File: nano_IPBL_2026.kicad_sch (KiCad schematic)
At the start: 21 parts, among them J1 DB301V-5.0-2P, M1 Motor_Servo, M10 Motor_Servo, M11 Motor_Servo, M12 Motor_Servo, M2 Motor_Servo, M3 Motor_Servo, M4 Motor_Servo, M5 Motor_Servo, M6 Motor_Servo, M7 Motor_Servo, M8 Motor_Servo, M9 Motor_Servo

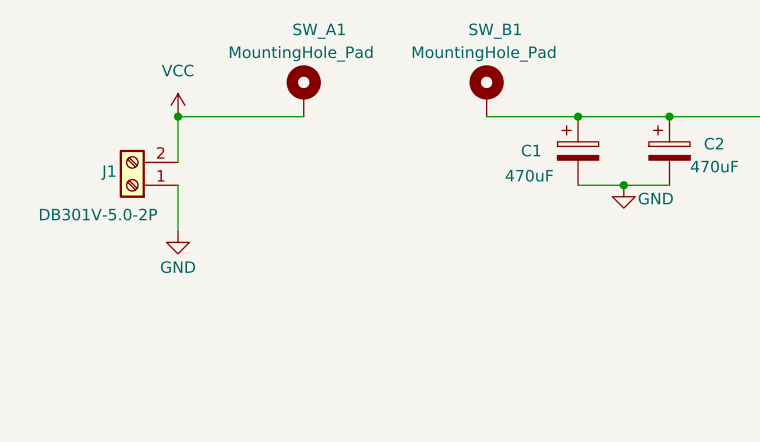
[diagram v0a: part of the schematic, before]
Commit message: Update screw terminal footprint and replace SW_A1/SW_B1 mounting holes with header
Screw terminal footprint now includes its 3D model counterpart. SW_A1
and SW_B1 mounting holes replaced with a 1-pin connected header.
Copper/silkscreen layer view colors changed from inverted to colored.
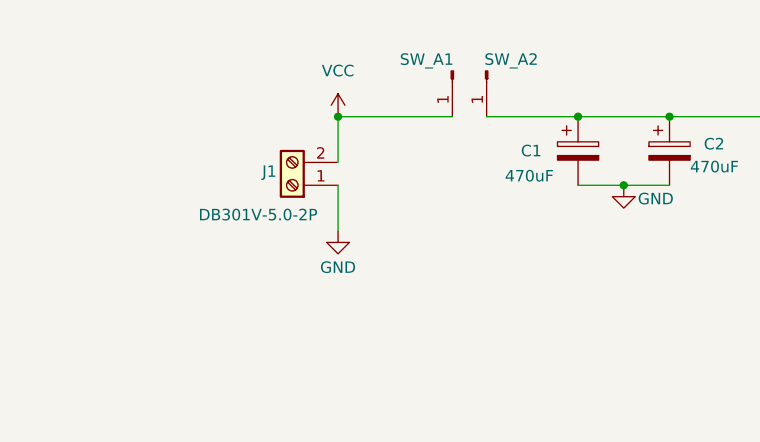
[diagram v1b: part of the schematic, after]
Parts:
- removed SW_A1, SW_B1: MountingHole_Pad, Arduino_MountingHole:MountingHole_1.2mm_M2_Pad_EDITED, symbol Mechanical:MountingHole_Pad
- added SW_A1, SW_A2: Conn_01x01_Pin, Connector_PinHeader_2.54mm:PinHeader_1x01_P2.54mm_Vertical, symbol Connector:Conn_01x01_Pin
- J1: footprint lcsc:CONN-TH_2P-P5.00_L7.6-W10.0 -> TerminalBlock_Phoenix:TerminalBlock_Phoenix_MKDS-1,5-2_1x02_P5.00mm_Horizontal
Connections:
- net Servo_IN: now also SW_A2.1 (Pin_1)
- net VCC: now also SW_A1.1 (Pin_1)
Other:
- moved on the sheet: J1
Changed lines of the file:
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@@
 	)
 	(junction
-		(at 40.64 39.37)
+		(at 58.42 39.37)
 		(diameter 0)
 		(color 0 0 0 0)
@@
 	(wire
 		(pts
-			(xy 40.64 39.37) (xy 40.64 44.45)
+			(xy 58.42 39.37) (xy 58.42 44.45)
 		)
 		(stroke
@@
 	(wire
 		(pts
-			(xy 40.64 39.37) (xy 54.61 39.37)
+			(xy 58.42 39.37) (xy 71.12 39.37)
 		)
 		(stroke
@@
 	(wire
 		(pts
-			(xy 40.64 46.99) (xy 40.64 52.07)
+			(xy 58.42 46.99) (xy 58.42 52.07)
 		)
 		(stroke
@@
 	(symbol
 		(lib_id "power:GND")
-		(at 40.64 52.07 0)
+		(at 58.42 52.07 0)
 		(unit 1)
 		(body_style 1)
@@
 		(dnp no)
 		(property "Reference" "#PWR02"
-			(at 40.64 58.42 0)
+			(at 58.42 58.42 0)
 			(hide yes)
 			(show_name no)
@@
 		)
 		(property "Value" "GND"
-			(at 40.64 56.134 0)
+			(at 58.42 56.134 0)
 			(show_name no)
 			(do_not_autoplace no)
@@
 		)
 		(property "Footprint" ""
-			(at 40.64 52.07 0)
+			(at 58.42 52.07 0)
 			(hide yes)
 			(show_name no)
@@
 		)
 		(property "Datasheet" ""
-			(at 40.64 52.07 0)
+			(at 58.42 52.07 0)
 			(hide yes)
 			(show_name no)
@@
 		)
 		(property "Description" "Power symbol creates a global label with name \"GND\" , ground"
-			(at 40.64 52.07 0)
+			(at 58.42 52.07 0)
 			(hide yes)
 			(show_name no)
@@
 	)
 	(symbol
-		(lib_id "Mechanical:MountingHole_Pad")
-		(at 74.93 36.83 0)
+		(lib_id "power:VCC")
+		(at 58.42 39.37 0)
 		(unit 1)
 		(body_style 1)
 		(exclude_from_sim no)
-		(in_bom no)
+		(in_bom yes)
 		(on_board yes)
 		(in_pos_files yes)
 		(dnp no)
-		(property "Reference" "SW_B1"
-			(at 72.898 29.718 0)
+		(fields_autoplaced yes)
+		(property "Reference" "#PWR01"
+			(at 58.42 43.18 0)
+			(hide yes)
 			(show_name no)
 			(do_not_autoplace no)
@@
 					(size 1.27 1.27)
 				)
-				(justify left)
 			)
 		)
-		(property "Value" "MountingHole_Pad"
-			(at 66.548 32.258 0)
+		(property "Value" "VCC"
+			(at 58.42 34.29 0)
 			(show_name no)
 			(do_not_autoplace no)
@@
 					(size 1.27 1.27)
 				)
-				(justify left)
 			)
 		)
-		(property "Footprint" "Arduino_MountingHole:MountingHole_1.2mm_M2_Pad_EDITED"
-			(at 74.93 36.83 0)
+		(property "Footprint" ""
+			(at 58.42 39.37 0)
 			(hide yes)
 			(show_name no)
@@
 		)
 		(property "Datasheet" ""
-			(at 74.93 36.83 0)
+			(at 58.42 39.37 0)
 			(hide yes)
 			(show_name no)
@@
 			)
 		)
-		(property "Description" "Mounting Hole with connection"
-			(at 74.93 36.83 0)
+		(property "Description" "Power symbol creates a global label with name \"VCC\""
+			(at 58.42 39.37 0)
 			(hide yes)
 			(show_name no)
@@
 			(project "nano_IPBL_2026"
 				(path "/0d35483a-0b12-46cc-b9f2-896fd6831779"
-					(reference "SW_B1")
+					(reference "#PWR01")
 					(unit 1)
 				)
@@
 	)
 	(symbol
-		(lib_id "power:VCC")
-		(at 40.64 39.37 0)
+		(lib_id "Connector:Conn_01x01_Pin")
+		(at 74.93 34.29 270)
 		(unit 1)
 		(body_style 1)
@@
 		(in_pos_files yes)
 		(dnp no)
-		(fields_autoplaced yes)
-		(property "Reference" "#PWR01"
-			(at 40.64 43.18 0)
-			(hide yes)
+		(property "Reference" "SW_A2"
+			(at 74.676 33.02 90)
 			(show_name no)
 			(do_not_autoplace no)
@@
 					(size 1.27 1.27)
 				)
+				(justify left)
 			)
 		)
-		(property "Value" "VCC"
-			(at 40.64 34.29 0)
+		(property "Value" "Conn_01x01_Pin"
+			(at 77.47 34.925 0)
+			(hide yes)
 			(show_name no)
 			(do_not_autoplace no)
@@
 			)
 		)
-		(property "Footprint" ""
-			(at 40.64 39.37 0)
+		(property "Footprint" "Connector_PinHeader_2.54mm:PinHeader_1x01_P2.54mm_Vertical"
+			(at 74.93 34.29 0)
 			(hide yes)
 			(show_name no)
@@
 		)
 		(property "Datasheet" ""
-			(at 40.64 39.37 0)
+			(at 74.93 34.29 0)
 			(hide yes)
 			(show_name no)
@@
 			)
 		)
-		(property "Description" "Power symbol creates a global label with name \"VCC\""
-			(at 40.64 39.37 0)
+		(property "Description" "Generic connector, single row, 01x01, script generated"
+			(at 74.93 34.29 0)
 			(hide yes)
 			(show_name no)
@@
 			(project "nano_IPBL_2026"
 				(path "/0d35483a-0b12-46cc-b9f2-896fd6831779"
-					(reference "#PWR01")
+					(reference "SW_A2")
 					(unit 1)
 				)
@@
 	)
 	(symbol
-		(lib_id "Mechanical:MountingHole_Pad")
-		(at 54.61 36.83 0)
-		(unit 1)
-		(body_style 1)
-		(exclude_from_sim no)
-		(in_bom no)
-		(on_board yes)
-		(in_pos_files yes)
-		(dnp no)
-		(property "Reference" "SW_A1"
-			(at 53.34 29.718 0)
-			(show_name no)
-			(do_not_autoplace no)
-			(effects
-				(font
-					(size 1.27 1.27)
-				)
-				(justify left)
-			)
-		)
-		(property "Value" "MountingHole_Pad"
-			(at 46.228 32.258 0)
-			(show_name no)
-			(do_not_autoplace no)
-			(effects
-				(font
-					(size 1.27 1.27)
-				)
-				(justify left)
-			)
-		)
-		(property "Footprint" "Arduino_MountingHole:MountingHole_1.2mm_M2_Pad_EDITED"
-			(at 54.61 36.83 0)
-			(hide yes)
-			(show_name no)
-			(do_not_autoplace no)
-			(effects
-				(font
-					(size 1.27 1.27)
-				)
-			)
-		)
-		(property "Datasheet" ""
-			(at 54.61 36.83 0)
-			(hide yes)
-			(show_name no)
-			(do_not_autoplace no)
-			(effects
-				(font
-					(size 1.27 1.27)
-				)
-			)
-		)
-		(property "Description" "Mounting Hole with connection"
-			(at 54.61 36.83 0)
-			(hide yes)
-			(show_name no)
-			(do_not_autoplace no)
-			(effects
-				(font
-					(size 1.27 1.27)
-				)
-			)
-		)
-		(pin "1"
-		)
-		(instances
-			(project "nano_IPBL_2026"
-				(path "/0d35483a-0b12-46cc-b9f2-896fd6831779"
-					(reference "SW_A1")
-					(unit 1)
-				)
-			)
-		)
-	)
-	(symbol
 		(lib_id "Motor:Motor_Servo")
 		(at 137.16 111.76 0)
@@
 	)
 	(symbol
+		(lib_id "Connector:Conn_01x01_Pin")
+		(at 71.12 34.29 270)
+		(unit 1)
+		(body_style 1)
+		(exclude_from_sim no)
+		(in_bom yes)
+		(on_board yes)
+		(in_pos_files yes)
+		(dnp no)
+		(property "Reference" "SW_A1"
+			(at 65.278 33.02 90)
+			(show_name no)
+			(do_not_autoplace no)
+			(effects
+				(font
+					(size 1.27 1.27)
+				)
+				(justify left)
+			)
+		)
+		(property "Value" "Conn_01x01_Pin"
+			(at 73.66 34.925 0)
+			(hide yes)
+			(show_name no)
+			(do_not_autoplace no)
+			(effects
+				(font
+					(size 1.27 1.27)
+				)
+			)
+		)
+		(property "Footprint" "Connector_PinHeader_2.54mm:PinHeader_1x01_P2.54mm_Vertical"
+			(at 71.12 34.29 0)
+			(hide yes)
+			(show_name no)
+			(do_not_autoplace no)
+			(effects
+				(font
+					(size 1.27 1.27)
+				)
+			)
+		)
+		(property "Datasheet" ""
+			(at 71.12 34.29 0)
+			(hide yes)
+			(show_name no)
+			(do_not_autoplace no)
+			(effects
+				(font
+					(size 1.27 1.27)
+				)
+			)
+		)
+		(property "Description" "Generic connector, single row, 01x01, script generated"
+			(at 71.12 34.29 0)
+			(hide yes)
+			(show_name no)
+			(do_not_autoplace no)
+			(effects
+				(font
+					(size 1.27 1.27)
+				)
+			)
+		)
+		(pin "1"
+		)
+		(instances
+			(project "nano_IPBL_2026"
+				(path "/0d35483a-0b12-46cc-b9f2-896fd6831779"
+					(reference "SW_A1")
+					(unit 1)
+				)
+			)
+		)
+	)
+	(symbol
 		(lib_id "Device:C_Polarized")
 		(at 95.25 43.18 0)
@@
 	(symbol
 		(lib_id "Connector:Screw_Terminal_01x02")
-		(at 35.56 46.99 180)
+		(at 53.34 46.99 180)
 		(unit 1)
 		(body_style 1)
@@
 		(dnp no)
 		(property "Reference" "J1"
-			(at 33.02 45.466 0)
+			(at 50.8 45.466 0)
 			(show_name no)
 			(do_not_autoplace no)
@@
 		)
 		(property "Value" "DB301V-5.0-2P"
-			(at 31.75 50.292 0)
+			(at 49.53 50.292 0)
 			(show_name no)
 			(do_not_autoplace no)
@@
 			)
 		)
-		(property "Footprint" "lcsc:CONN-TH_2P-P5.00_L7.6-W10.0"
-			(at 35.56 46.99 0)
+		(property "Footprint" "TerminalBlock_Phoenix:TerminalBlock_Phoenix_MKDS-1,5-2_1x02_P5.00mm_Horizontal"
+			(at 53.34 46.99 0)
 			(hide yes)
 			(show_name no)
@@
 		)
 		(property "Datasheet" ""
-			(at 35.56 46.99 0)
+			(at 53.34 46.99 0)
 			(hide yes)
 			(show_name no)
@@
 		)
 		(property "Description" "Generic screw terminal, single row, 01x02, script generated (kicad-library-utils/schlib/autogen/connector/)"
-			(at 35.56 46.99 0)
+			(at 53.34 46.99 0)
 			(hide yes)
 			(show_name no)
@@
 		)
 		(property "LCSC Part" "C395882"
-			(at 35.56 46.99 0)
+			(at 53.34 46.99 0)
 			(hide yes)
 			(show_name no)
